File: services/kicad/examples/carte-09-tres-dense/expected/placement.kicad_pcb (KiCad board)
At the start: 2 copper layers, 130 x 100 mm, 62 parts, among them J1 IN_5V, J10 IO0, J11 IO1, J12 IO2, J13 IO3, J14 IO4, J2 SWD, U1 STM32F103C8T6, U2 AMS1117-3.3

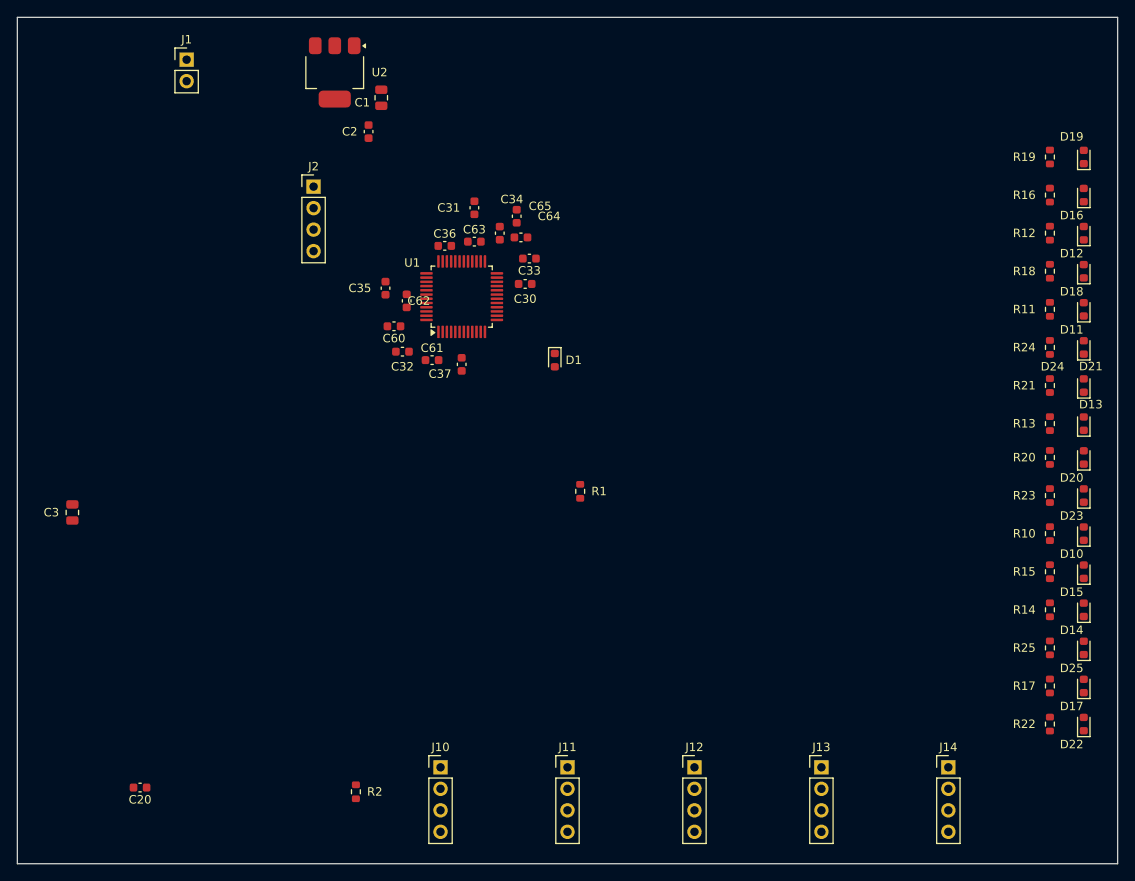
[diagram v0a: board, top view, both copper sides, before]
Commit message: fix(kicad): plan de masse referme — banc DIX cartes sur dix, 0 erreur 0 manquante (#237)
* docs(kicad): la derniere rupture de plan tient a UN segment, pas a un faisceau

Diagnostic complet du seul defaut restant du banc (carte-10), mesure sur le
board qui le porte vraiment, apres consultation de Codex et de GLM.

Mesures sur `/tmp/livr/carte-10-maximale/route.kicad_pcb` (33 violations,
0 erreur, 1 connexion manquante) :

- 23 ilots GND sur les deux faces, exactement 2 orphelins, et ce sont des
  JUMEAUX : F.Cu 1,30 mm2 (porte la pastille C35.2) et B.Cu 0,99 mm2.
- AUCUN de leurs points n a le plan principal en vis-a-vis : ils se font face
  l un l autre. La piste « changer de face par un via », proposee par GLM, est
  donc REFUTEE par la mesure.
- La couture de production visite les deux ilots et refuse la totalite de
  leurs sites (23 et 18 candidats ; obstacle 16/10, hors_polygone 6/7,
  trou_trop_pres 1/1) : un via ne tient pas dans un millimetre carre.
  Le raccord par courte piste rend relies 0, sans_chemin 19.
- Mais le plan principal n est qu a 0,862 mm sur F.Cu et 0,781 mm sur B.Cu, et
  UN SEUL segment coupe le couloir de chaque face (EXT2_1, EXT4_1).

Le plan de Codex — deplacer l obstacle au lieu de chercher un passage a
travers — a donc ici un ensemble a arracher d UN segment par face, pas une
recherche ouverte. Decision de strategie de routage : D-2026-09-22-a, EN
ATTENTE. Rien n est implemente.

Levier natif verifie et jamais appele : LocalRerouter.reroute_segment() de
kicad-tools, utilise par drc/repair_clearance.py, zero appelant Cirqix. Il
travaille sur le document S-expression quand notre code travaille sur pcbnew.

Lecons inscrites dans CLAUDE.md :
- j ai d abord mesure le board VERSIONNE du 21, qui est propre (non_connectes
  0) et se pretait a toutes les demonstrations — un via y tenait avec 0,29 mm
  de marge. Verifier que l artefact PORTE le defaut avant de le diagnostiquer.
- ma premiere sonde raisonnait zone par zone, alors que la carte por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
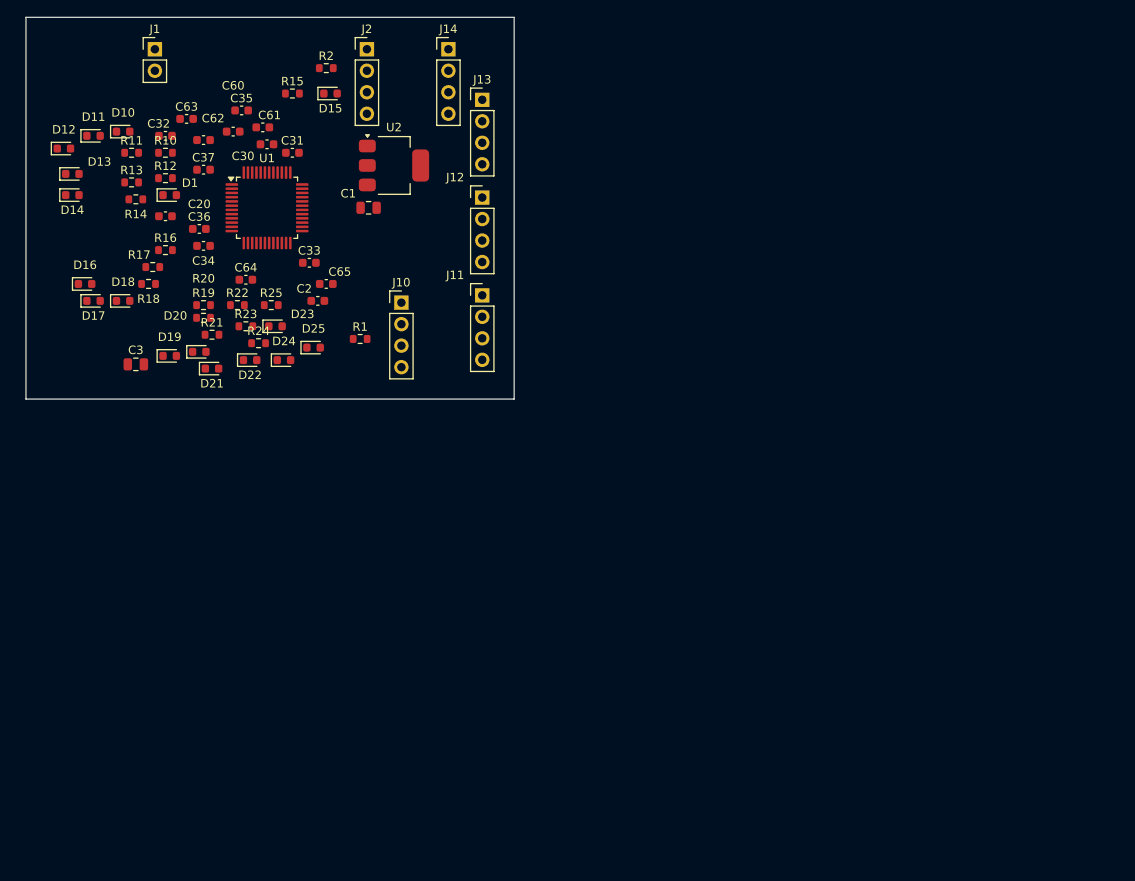
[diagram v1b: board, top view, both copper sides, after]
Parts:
- moved D14 129.2 mm to (90.0, 76.0), turned to 0 degrees
- moved D17 125.5 mm to (92.5, 88.5), turned to 0 degrees
- moved D13 123.1 mm to (90.0, 73.5), turned to 0 degrees
- moved D10 123.0 mm to (96.0, 68.5), turned to 0 degrees
- moved D12 120.9 mm to (89.0, 70.5), turned to 0 degrees
- moved D11 118.8 mm to (92.5, 69.0), turned to 0 degrees
- moved D16 118.5 mm to (91.5, 86.5), turned to 0 degrees
- moved R14 118.4 mm to (97.5, 76.5), turned to 0 degrees
- moved R17 117.0 mm to (99.5, 84.5), turned to 0 degrees
- moved R10 113.8 mm to (101.0, 71.0), turned to 0 degrees
- moved D18 113.6 mm to (96.0, 88.5), turned to 0 degrees
- moved R13 112.2 mm to (97.0, 74.5), turned to 0 degrees
- moved D19 110.5 mm to (101.5, 95.0), turned to 0 degrees
- moved R11 110.1 mm to (97.0, 71.0), turned to 0 degrees
- moved R22 108.0 mm to (109.5, 89.0), turned to 0 degrees
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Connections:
- U1 pad 36: Net-(U1-36) -> PWR_FLAG
- U1 pad 48: Net-(U1-48) -> PWR_FLAG
- U1 pad 9: IO_L5 -> PWR_FLAG
- U2 pad 3: VIN -> PWR_FLAG
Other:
- board size 130 x 100 mm -> 57.7 x 45.1 mm
